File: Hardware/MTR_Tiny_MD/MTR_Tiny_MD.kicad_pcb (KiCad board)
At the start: 6 copper layers, 49.9 x 49.9 mm, 83 parts, among them J1 USB_C_Receptacle_USB2.0, J2 68021-412HLF, J3 LED OUT, J4 UART, J5 LED OUT, J6 XT30PB, Q1 AO3401A, SW1 Boot, SW2 Reset, U1 RP2040, U2 W25Q16JVUXIQ, U3 LMR36506, U4 TPS71933-33DRVR, U5 DRV8316RQRGFRQ1, U6 AS5600L-ASOM, Y1 8Z-12.000MAAJ-T

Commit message: add drawing.io and footprint & 3D model to project
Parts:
- C1, C10, C11, C13, C18, C2, C20, C3, C30, C32, C34, C35, C4, C5, C6, C7, C8, C9, R1, R11, R12, R14, R15, R16, R2, R3, R4, R5, R6, R7, R8, R9: footprint Capacitor_SMD:C_0402_1005Metric -> C_0402_1005Metric
- C12, C15, C16, C17, C19, C21, C22, C23, C24, C25, C26, C27, C28, C36, C37: footprint Capacitor_SMD:C_0603_1608Metric -> C_0603_1608Metric
- C14: footprint Capacitor_SMD:C_0805_2012Metric -> C_0805_2012Metric
- C29, C31, C33: footprint Capacitor_SMD:C_0201_0603Metric -> C_0201_0603Metric
- D1: footprint LED_SMD:LED_WS2812B_PLCC4_5.0x5.0mm_P3.2mm -> LED_WS2812B_PLCC4_5.0x5.0mm_P3.2mm
- D2, D3: footprint LED_SMD:LED_0603_1608Metric -> LED_0603_1608Metric
- G***: footprint Personal:logoMTR -> logoMTR
- G12: footprint Personal:KiCad -> KiCad
- H1, H3, H8, H9: footprint MountingHole:MountingHole_3.2mm_M3_Pad_Via -> MountingHole_3.2mm_M3_Pad_Via
- H10, H11, H12: footprint Personal:Motor_Wire_Solder_Pad -> Motor_Wire_Solder_Pad
- H6, H7: footprint TestPoint:TestPoint_Pad_1.5x1.5mm -> TestPoint_Pad_1.5x1.5mm
- J1: footprint Connector_USB:USB_C_Receptacle_HRO_TYPE-C-31-M-12 -> USB_C_Receptacle_HRO_TYPE-C-31-M-12
- J2: footprint PinHeader:PinHeader_2x06_P2.54mm_Vertical -> PinHeader_2x06_P2.54mm_Vertical
- J3, J4, J5: footprint PinHeader:PinHeader_1x02_P2.54mm_Vertical -> PinHeader_1x02_P2.54mm_Vertical
- J6: footprint Personal:XT30PB -> XT30PB
- L1: footprint Inductor_SMD:L_1210_3225Metric -> L_1210_3225Metric
- Q1: footprint digikey-footprints:SOT-23-3 -> SOT-23-3
- R13: footprint Resistor_SMD:R_0603_1608Metric -> R_0603_1608Metric
- SW1, SW2: footprint Personal:TVBM17 -> TVBM17
- U1: footprint Package_DFN_QFN:QFN-56-1EP_7x7mm_P0.4mm_EP3.2x3.2mm -> QFN-56-1EP_7x7mm_P0.4mm_EP3.2x3.2mm
- U2: footprint Personal:W25Q16JVUXIQ -> W25Q16JVUXIQ
- U3: footprint Personal:LMR36506 -> LMR36506
- U4: footprint Personal:TPS71933-33DRVR -> TPS71933-33DRVR
- U5: footprint Personal:DRV8316RQRGFRQ1 -> DRV8316RQRGFRQ1
- U6: footprint Personal:AS5600L-ASOM -> AS5600L-ASOM
- Y1: footprint SamacSys_Parts:8Z12000MAAJT -> 8Z12000MAAJT
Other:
- board text added: "02"
- board text added: "03"
- board text added: "09"
- board text added: "20"
- board text added: "21"
- board text added: "22"
- board text added: "24"
- board text added: "25"
- board text added: "USB-C"
- board text removed: "USB C"

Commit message: Add new Vbuck
LMR36506 to MAX15462AATA+T
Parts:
- removed C14: 2.2uF 50v, C_0805_2012Metric
- removed C15, C19: 100nF 50v, C_0603_1608Metric
- removed C16: 1uF 16v, C_0603_1608Metric
- removed C21, C23: 22uF 10v, C_0603_1608Metric
- removed L1: 15uH, L_1210_3225Metric
- removed U3: LMR36506, LMR36506
- added C38: 1uF 50V, Capacitor_SMD:C_1206_3216Metric, F.Cu at (105.1, 83.1)
- added C39: 1uF 50V, Capacitor_SMD:C_1206_3216Metric, F.Cu at (100.2, 84.3)
- added C40: 10uF 10V, Capacitor_SMD:C_1206_3216Metric, F.Cu at (100.2, 86.9)
- added C41: 22uF 10v, Capacitor_SMD:C_0603_1608Metric, F.Cu at (104.3, 89.4)
- added C42: 22uF 10v, Capacitor_SMD:C_0603_1608Metric, F.Cu at (107.1, 88.7)
- added F1: 500mA, Fuse:Fuse_0603_1608Metric, F.Cu at (115.2, 108.1)
- added F2: 250mA, Fuse:Fuse_0603_1608Metric, F.Cu at (113.5, 85.2)
- added L2: 33uH, Inductor_SMD:L_1210_3225Metric, F.Cu at (109.3, 86.0)
- added U7: MAX15462AATA+T, footprints:21-0487_T822CN&plus_1_MXM, F.Cu at (104.9, 86.1)
- C1, C10, C11, C13, C18, C2, C20, C3, C30, C32, C34, C35, C4, C5, C6, C7, C8, C9: footprint C_0402_1005Metric -> Capacitor_SMD:C_0402_1005Metric
- C12, C17, C22, C24, C25, C26, C27, C28, C37: footprint C_0603_1608Metric -> Capacitor_SMD:C_0603_1608Metric
- C29, C31, C33: footprint C_0201_0603Metric -> Capacitor_SMD:C_0201_0603Metric
- C36: value 1.3uF -> 2u2F; footprint C_0603_1608Metric -> Capacitor_SMD:C_0603_1608Metric
- D1: footprint LED_WS2812B_PLCC4_5.0x5.0mm_P3.2mm -> LED_SMD:LED_WS2812B_PLCC4_5.0x5.0mm_P3.2mm
- D2, D3: footprint LED_0603_1608Metric -> LED_SMD:LED_0603_1608Metric
- H1, H3, H8, H9: footprint MountingHole_3.2mm_M3_Pad_Via -> MountingHole:MountingHole_3.2mm_M3_Pad_Via
- H10, H11, H12: footprint Motor_Wire_Solder_Pad -> Personal:Motor_Wire_Solder_Pad
- H6, H7: footprint TestPoint_Pad_1.5x1.5mm -> TestPoint:TestPoint_Pad_1.5x1.5mm
- J1: footprint USB_C_Receptacle_HRO_TYPE-C-31-M-12 -> Connector_USB:USB_C_Receptacle_HRO_TYPE-C-31-M-12
- J2: footprint PinHeader_2x06_P2.54mm_Vertical -> PinHeader:PinHeader_2x06_P2.54mm_Vertical
- J3, J4, J5: footprint PinHeader_1x02_P2.54mm_Vertical -> PinHeader:PinHeader_1x02_P2.54mm_Vertical
- J6: footprint XT30PB -> Personal:XT30PB
- Q1: footprint SOT-23-3 -> digikey-footprints:SOT-23-3
- R1, R11, R12, R14, R15, R16, R2, R3, R4, R5, R6, R7, R8, R9: footprint C_0402_1005Metric -> Resistor_SMD:R_0402_1005Metric
- R13: footprint R_0603_1608Metric -> Resistor_SMD:R_0603_1608Metric
- SW1, SW2: footprint TVBM17 -> Personal:TVBM17
- U1: footprint QFN-56-1EP_7x7mm_P0.4mm_EP3.2x3.2mm -> Package_DFN_QFN:QFN-56-1EP_7x7mm_P0.4mm_EP3.2x3.2mm
- U2: footprint W25Q16JVUXIQ -> Personal:W25Q16JVUXIQ
- U4: footprint TPS71933-33DRVR -> Personal:TPS71933-33DRVR
- U5: footprint DRV8316RQRGFRQ1 -> Personal:DRV8316RQRGFRQ1
- U6: footprint AS5600L-ASOM -> Personal:AS5600L-ASOM
- Y1: footprint 8Z12000MAAJT -> SamacSys_Parts:8Z12000MAAJT
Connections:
- J2 pad 9: GND -> unconnected-(J2-Pad9)
- U4 pad 2: V_USB -> Net-(U4-EN1)
- U4 pad 6: V_USB -> Net-(U4-EN1)
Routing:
- net ALIM: track 44.7 -> 17.0 mm
- net 3V3_BUCK: track 152.5 -> 134.9 mm, vias 58 -> 55
- net FeedBack: track 0.00 -> 15.7 mm
- net Net-(C16-Pad1): track 14.9 -> 0.00 mm, vias 2 -> 0
- net GND: track 205.7 -> 193.0 mm, vias 86 -> 74
- net Net-(C19-Pad2): track 5.62 -> 0.00 mm
- net Net-(U7-VCC): track 0.00 -> 3.35 mm
- net Net-(C19-Pad1): track 2.50 -> 0.00 mm
- net Net-(U7-LX): track 0.00 -> 2.32 mm

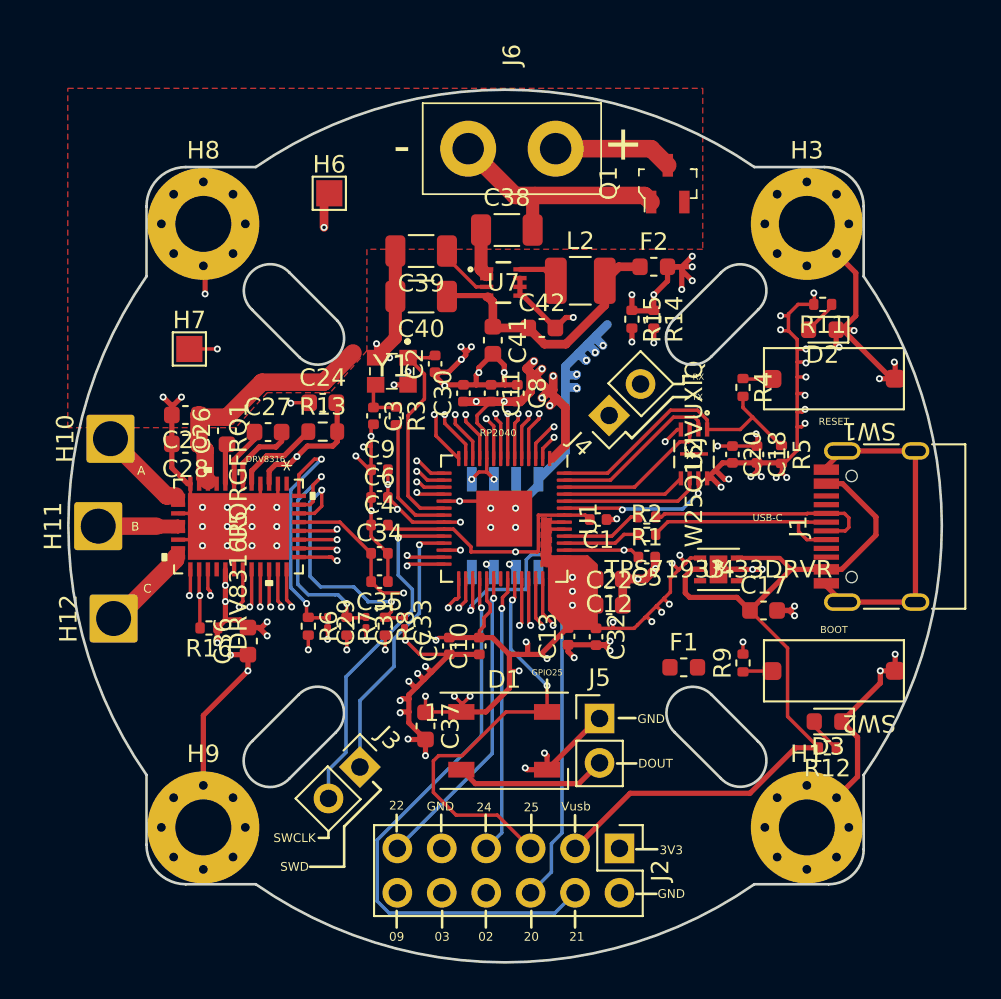
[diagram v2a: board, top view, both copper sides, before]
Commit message: Silkscreen labelling - RFP
Ready For Production Rev 1.1
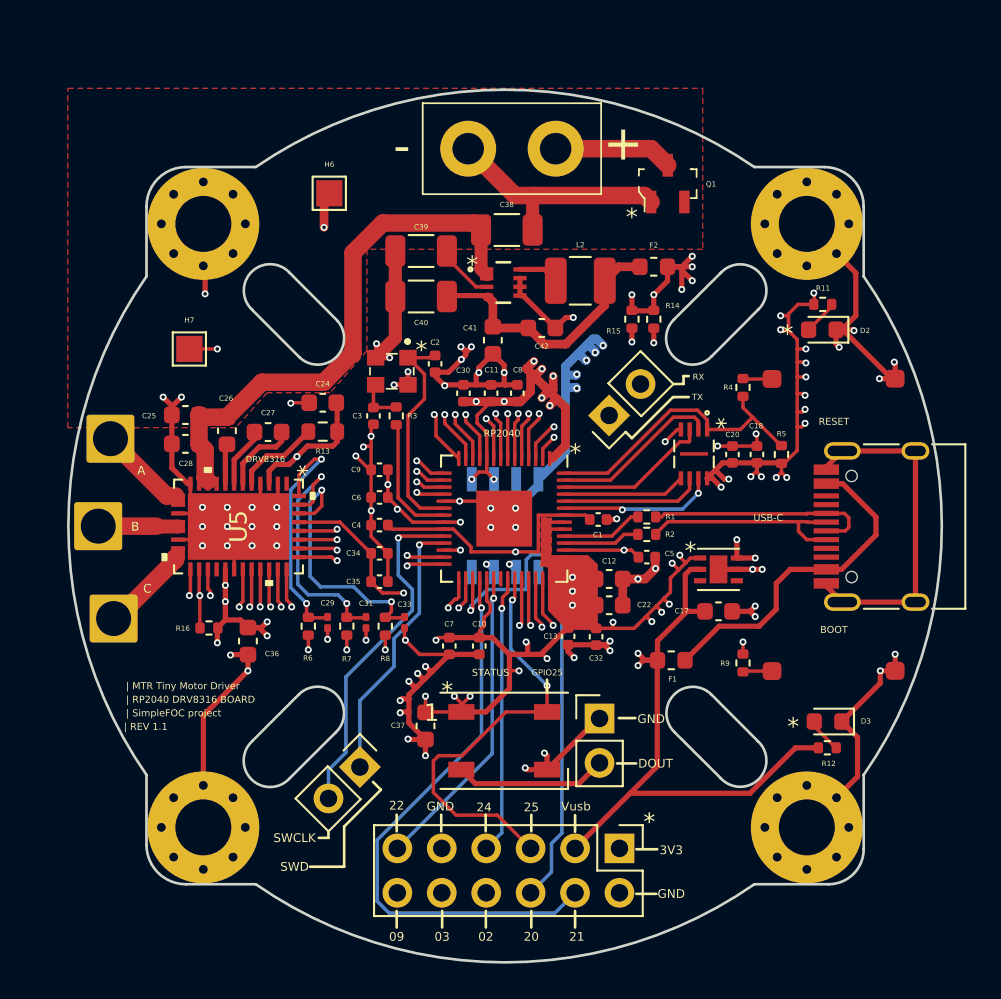
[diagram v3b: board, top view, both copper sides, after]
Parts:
- removed G12: LOGO, KiCad
- added REF**: LOGO, Library:KiCad, F.Cu at (93.5, 100.2)
- moved G*** 18.0 mm to (116.6, 100.5)
- moved C17 2.58 mm to (117.2, 104.9)
- moved F1 0.82 mm to (114.5, 107.7), turned to 180 degrees
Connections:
- F1 pad 1: V_USB -> Net-(F1-Pad1)
- F1 pad 2: Net-(U4-EN1) -> V_USB
- J1 pad A4: V_USB -> Net-(F1-Pad1)
- J1 pad A9: V_USB -> Net-(F1-Pad1)
- J1 pad B4: V_USB -> Net-(F1-Pad1)
- J1 pad B9: V_USB -> Net-(F1-Pad1)
- U4 pad 2: Net-(U4-EN1) -> V_USB
- U4 pad 6: Net-(U4-EN1) -> V_USB
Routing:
- net Net-(F1-Pad1): track 0.00 -> 19.4 mm
- net ALIM: track 17.0 -> 31.0 mm
- net V_USB: track 48.9 -> 54.9 mm, vias 0 -> 4
- net GND: track 193.0 -> 191.5 mm
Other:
- board text added: "*"
- board text added: "STATUS"
- board text added: "locked"
- board text added: "| MTR Tiny Motor Driver"
- board text added: "| REV 1.1"
- board text added: "| RP2040 DRV8316 BOARD"
- board text added: "| SimpleFOC project"

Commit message: add usb C PD controler
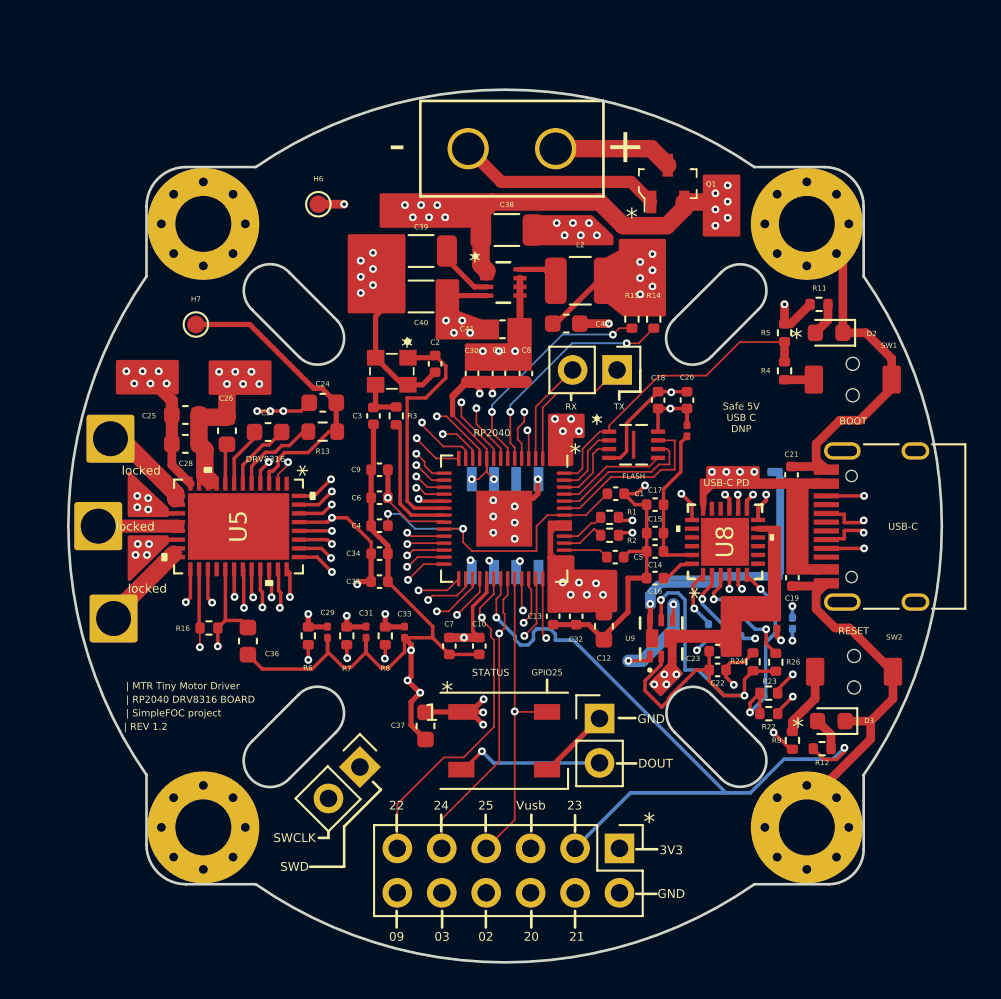
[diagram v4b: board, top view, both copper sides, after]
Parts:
- removed F1: 500mA, Fuse:Fuse_0603_1608Metric
- removed F2: 250mA, Fuse:Fuse_0603_1608Metric
- removed U4: TPS71933-33DRVR, Personal:TPS71933-33DRVR
- added 3v3ToVddd1: 3V3toVddJumper, Resistor_SMD:R_0201_0603Metric, F.Cu at (115.4, 94.6)
- added C14: 4.7uF, Capacitor_SMD:C_0402_1005Metric, F.Cu at (113.6, 101.5)
- added C15: 100nF, Capacitor_SMD:C_0402_1005Metric, F.Cu at (113.6, 100.4)
- added C16: 4.7uF, Capacitor_SMD:C_0402_1005Metric, F.Cu at (113.6, 103.0)
- added C19: 4.7uF, Capacitor_SMD:C_0402_1005Metric, F.Cu at (121.4, 103.0)
- added C21: 100nF, Capacitor_SMD:C_0402_1005Metric, F.Cu at (121.4, 97.1)
- added C23: DNF, Capacitor_SMD:C_0402_1005Metric, F.Cu at (117.2, 107.2)
- added Coarse1: CurrentSelect, Resistor_SMD:R_0201_0603Metric, B.Cu at (121.4, 105.6)
- added JP8: +VBUS_OUT, Resistor_SMD:R_0201_0603Metric, F.Cu at (120.5, 105.6)
- added R22: 1k, Resistor_SMD:R_0402_1005Metric, F.Cu at (120.1, 110.8)
- added R23: 5.1k, Resistor_SMD:R_0402_1005Metric, F.Cu at (120.1, 109.6)
- added R24: 20k, Resistor_SMD:R_0402_1005Metric, F.Cu at (119.2, 107.8)
- added R26: 2k2, Resistor_SMD:R_0402_1005Metric, F.Cu at (120.5, 107.8)
- added U8: CYPD3177-24LQXQT, footprints:CYPD3177-24LQXQT_CYP, F.Cu at (117.6, 100.9)
- added U9: SIA931DJ-T1-GE3, footprints:MOSFET_T1-GE3_VIS, F.Cu at (113.9, 106.5)
- added Vbus1: VbusJumper, Resistor_SMD:R_0201_0603Metric, B.Cu at (120.2, 97.2)
- added VbusMax1: VbusMax, Resistor_SMD:R_0201_0603Metric, B.Cu at (118.1, 106.3)
- added VbusMin1: VbusMin, Resistor_SMD:R_0201_0603Metric, B.Cu at (116.6, 106.0)
- C17: value 10uF -> 100nF; footprint Capacitor_SMD:C_0603_1608Metric -> Capacitor_SMD:C_0402_1005Metric
- C22: value 10uF -> 4.7uF; footprint Capacitor_SMD:C_0603_1608Metric -> Capacitor_SMD:C_0402_1005Metric
- D3: value USB ON -> LED
- H6, H7: footprint TestPoint:TestPoint_Pad_1.5x1.5mm -> TestPoint:TestPoint_Pad_D1.0mm
- J6: footprint Personal:XT30PB -> footprints:CONN_XT30UPB-M_AMA
- R5: value 1k -> DNF
- SW1, SW2: footprint Personal:TVBM17 -> Button_Switch_additional:TVAF06-A020B-R
- moved G*** 26.1 mm to (90.5, 99.7)
- moved REF** 16.8 mm to (105.2, 88.2)
- moved C22 7.22 mm to (117.2, 108.2), turned to 180 degrees
- moved C17 7.10 mm to (113.6, 98.8), turned to 180 degrees
- moved R5 6.96 mm to (121.0, 89.0), turned to 90 degrees
- moved C18 6.45 mm to (113.8, 92.8)
- moved R9 5.25 mm to (121.4, 112.3), turned to -90 degrees
- moved C20 4.05 mm to (115.4, 92.8)
- moved U2 3.49 mm to (112.3, 95.4), turned to 0 degrees
- moved C12 2.72 mm to (110.7, 105.8), turned to 90 degrees
- moved J4 2.64 mm to (111.4, 91.1), turned to -90 degrees
- moved R4 2.56 mm to (121.0, 91.2), turned to 90 degrees
- moved R2 2.13 mm to (111.0, 100.5)
- moved R1 2.13 mm to (111.0, 99.5)
- moved C5 1.80 mm to (111.3, 101.8)
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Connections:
- net Net-(F1-Pad1) renamed +VBUS
- C17 pad 1: V_USB -> VDDD
- C22 pad 1: 3V3_BUCK -> DRAIN_1
- C22 pad 2: GND -> GATE
- C40 pad 1: FeedBack -> 3V3_BUCK
- C41 pad 1: FeedBack -> 3V3_BUCK
- C42 pad 1: FeedBack -> 3V3_BUCK
- J1 pad A5: unconnected-(J1-CC1-PadA5) -> /CC1
- J1 pad A6: USB_D+ -> unconnected-(J1-D+-PadA6)
- J1 pad A7: USB_D- -> unconnected-(J1-D--PadA7)
- J1 pad B5: unconnected-(J1-CC2-PadB5) -> /CC2
- J1 pad S1: GND -> unconnected-(J1-SHIELD-PadS1)
- J2 pad 3: V_USB -> GPIO23
- J2 pad 5: GPIO25 -> +VBUS_OUT
- J2 pad 7: GPIO24 -> GPIO25
- J2 pad 9: unconnected-(J2-Pad9) -> GPIO24
- L2 pad 2: FeedBack -> 3V3_BUCK
- R12 pad 2: V_USB -> GPIO23
- U1 pad 35: unconnected-(U1-GPIO23-Pad35) -> GPIO23
- U5 pad 41: GND -> unconnected-(U5-EPAD-Pad41)
- U7 pad 4: FeedBack -> 3V3_BUCK
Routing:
- net V_USB: track 54.9 -> 0.00 mm, vias 4 -> 0
- net ALIM: track 31.0 -> 85.5 mm, vias 0 -> 19
- net GPIO23: track 0.00 -> 41.2 mm, vias 0 -> 2
- net 3V3_BUCK: track 134.9 -> 95.0 mm, vias 55 -> 36
- net +VBUS_OUT: track 0.00 -> 32.2 mm, vias 0 -> 4
- net DRAIN_1: track 0.00 -> 27.2 mm, vias 0 -> 2
- net GATE: track 0.00 -> 25.3 mm, vias 0 -> 2
- net I2C_SDA: track 22.7 -> 41.1 mm, vias 3 -> 4
- net FeedBack: track 15.7 -> 0.00 mm
- net I2C_SCL: track 26.2 -> 40.9 mm, vias 3 -> 4
- net /CC1: track 0.00 -> 14.1 mm, vias 0 -> 2
- net ISNK_FINE: track 0.00 -> 11.6 mm, vias 0 -> 2
- net /CC2: track 0.00 -> 10.7 mm, vias 0 -> 2
- net GPIO21: track 33.0 -> 24.0 mm
- net VDDD: track 0.00 -> 8.85 mm
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- removed copper zone on F.Cu, net 3V3_BUCK
- removed copper zone on F.Cu, net ALIM
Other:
- board text added: "23"
- board text added: "FLASH"
- board text added: "Safe 5V USB C DNP"
- board text added: "SimpleFOC"
- board text added: "USB-C PD"
- board text added: "XT30P"
- board text added: "| REV 1.2"
- board text removed: "A"
- board text removed: "B"
- board text removed: "C"
- board text removed: "| REV 1.1"

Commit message: Update design, add PD controler, correct SPI
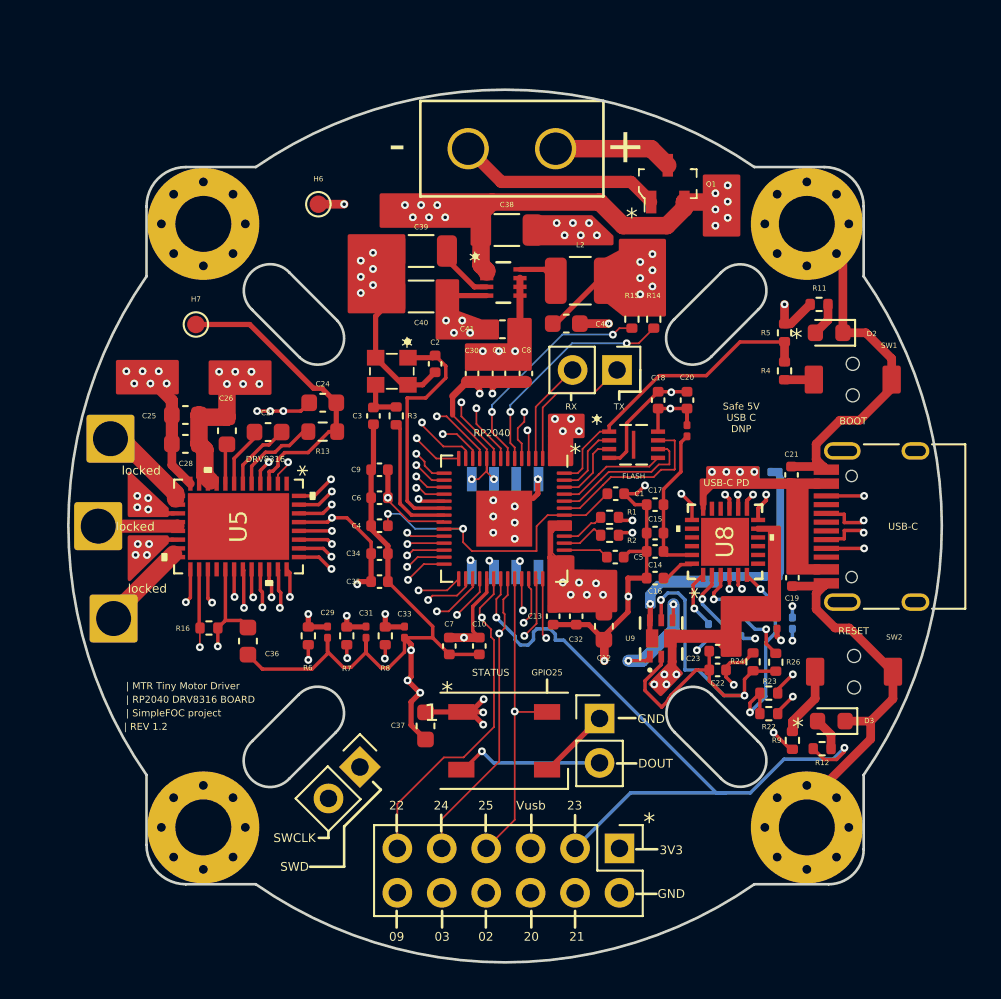
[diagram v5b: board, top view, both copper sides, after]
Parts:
- R16: value 100R -> 5.1k
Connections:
- U5 pad 33: SPI_MOSI -> SPI_MISO
- U5 pad 34: SPI_MISO -> SPI_MOSI
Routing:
- net SPI_MOSI: track 11.3 -> 12.8 mm
- net GND: track 182.7 -> 183.9 mm, vias 52 -> 54
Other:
- board text removed: "SimpleFOC"

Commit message: Update 1.2.2
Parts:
- added C44: 2u2, Capacitor_SMD:C_0402_1005Metric, F.Cu at (117.1, 118.1)
- added R19: 5.1k, Resistor_SMD:R_0402_1005Metric, F.Cu at (116.3, 115.7)
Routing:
- net RUN: track 28.9 -> 37.1 mm, vias 2 -> 3
- net +1V1: track 20.4 -> 28.3 mm, vias 2 -> 3
- net 3V3_BUCK: track 95.0 -> 101.8 mm
- net GND: track 183.9 -> 187.3 mm
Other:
- board text added: "| REV 1.2.2"
- board text removed: "| REV 1.2"
